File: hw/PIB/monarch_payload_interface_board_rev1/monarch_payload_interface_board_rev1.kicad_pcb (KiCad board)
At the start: 4 copper layers, 96 x 89.9 mm, 187 parts, among them J1 5037630291, J10 5037630491, J11 5037630691, J12 5037630691, J13 5037630491, J14 5037630491, J15 5037630691, J16 20021121-00008C4LF, J2 5037630291, J3 5037630691, J4 5037630691, J5 5037630691, J6 5037630691, J7 5037630691, J8 5037630691, J9 5037630491, Q1 FZT600TA, Q10 FZT600TA, Q11 FZT600TA, Q12 FZT600TA, Q13 FZT600TA, Q14 FZT600TA, Q15 FZT600TA, Q16 FZT600TA, Q17 FZT600TA, Q18 FZT600TA, Q19 FZT600TA, Q2 FZT600TA, Q3 FZT600TA, Q4 FZT600TA, Q5 FZT600TA, Q6 FZT600TA, Q7 FZT600TA, Q8 FZT600TA, Q9 FZT600TA, U1 Payload, U10 AD7124-8BCPZ-RL, U11 WSK06121L000FEA, U12 WSK06121L000FEA, U13 WSK06121L000FEA, U14 WSK06121L000FEA, U2 STM32L4A6VGTx, U3 MAX31856MUD_T, U4 TPS61088QRHLRQ1, U5 MAX31856MUD_T, U6 MAX31856MUD_T, U7 MAX31856MUD_T, U8 MAX31856MUD_T, U9 AD7124-8BCPZ-RL

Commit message: more minor tweaks
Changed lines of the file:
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@@
 		(polygon
 			(pts
-				(xy 51.29 70.12) (xy 51.29 83.17) (xy 51.04 83.42) (xy 51.04 101.62) (xy 51.06 101.64) (xy 121.15 101.64)
+				(xy 51.29 70.12) (xy 50.95 82.55) (xy 50.59 83.87) (xy 50.59 101.17) (xy 51.06 101.64) (xy 121.15 101.64)
 				(xy 121.51 101.28) (xy 121.51 70.69) (xy 64.88 70.69) (xy 62.9 72.67) (xy 55.73 72.67) (xy 53.57 70.51)
 				(xy 53.57 70.12)
@@
 			(pts
 				(xy 62.9832 46.3172) (xy 67.6314 46.3172) (xy 67.6568 46.2918) (xy 67.6568 42.8882) (xy 67.6314 42.8628)
-				(xy 65.7518 42.8628) (xy 64.2532 41.3642) (xy 64.05 41.3642) (xy 64.05 42.1516) (xy 63.923 42.2786)
+				(xy 65.7518 42.8628) (xy 64.2532 41.3642) (xy 64.05 41.3642) (xy 64.05 41.9516) (xy 63.723 42.2786)
 				(xy 62.9832 42.2786)
 			)

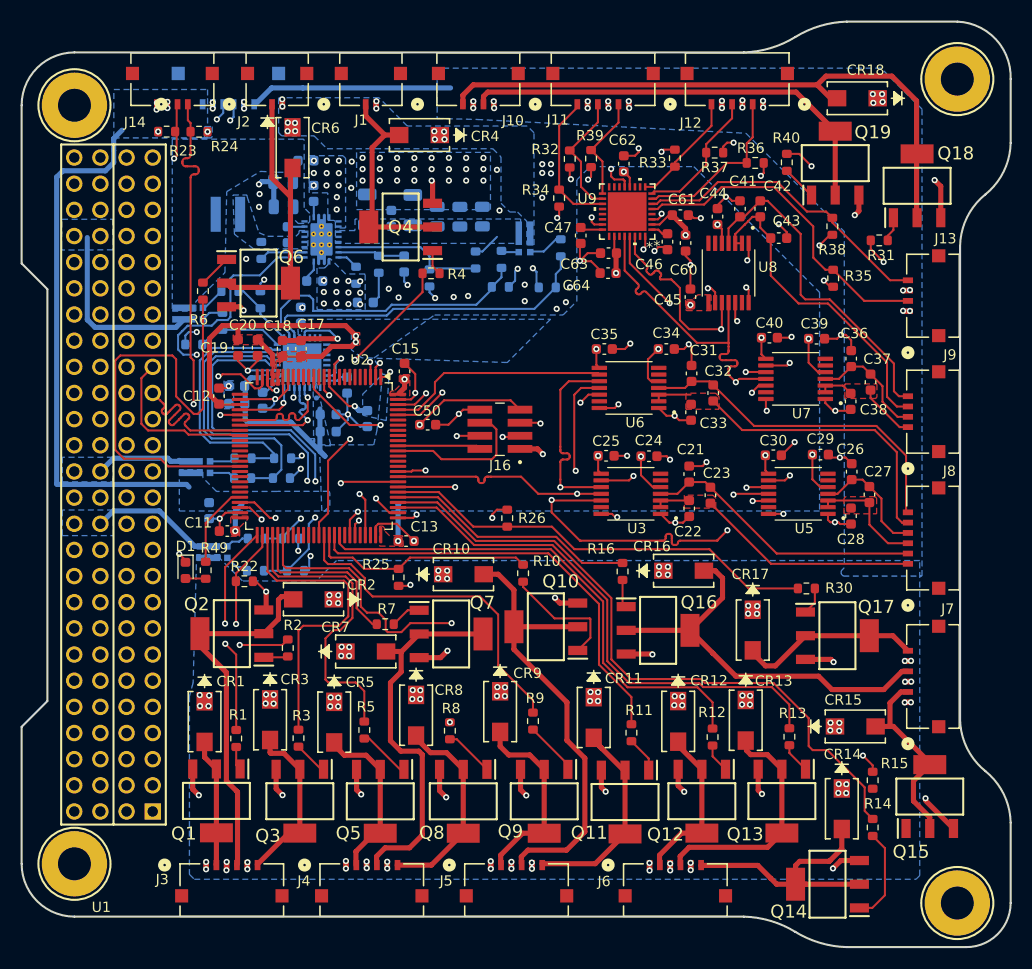
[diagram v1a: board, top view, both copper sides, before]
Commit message: fixed vias
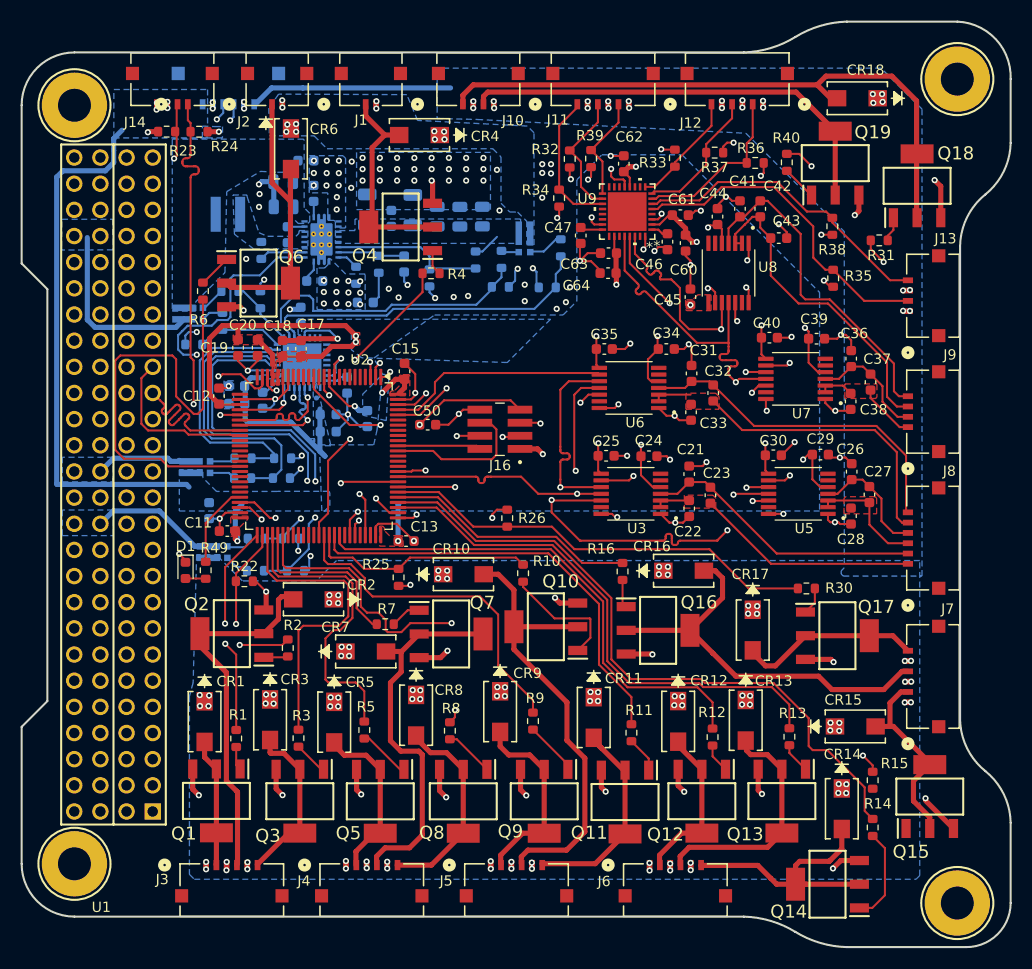
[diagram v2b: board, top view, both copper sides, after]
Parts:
- R49: value 1k -> 125
- moved CR6 0.19 mm to (60.5, 30.7)
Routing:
- net +3V3: track 164.7 -> 187.2 mm

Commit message: PIB Signature
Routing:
- net GND: vias 154 -> 156
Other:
- board text added: "MonARCH Payload Interface Board Rev. 1 SIROTA 3/12/2026"
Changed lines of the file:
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@@
 		(tags "capacitor")
 		(property "Reference" "C15"
-			(at 2.185 0.08 0)
+			(at -0.235 2.52 0)
 			(layer "F.SilkS")
 			(effects
@@
 		)
 	)
+	(gr_rect
+		(start 68.25 47)
+		(end 87.75 50.4)
+		(stroke
+			(width 0.1)
+			(type default)
+		)
+		(fill no)
+		(layer "F.SilkS")
+	)
+	(gr_text "MonARCH Payload Interface Board Rev. 1\nSIROTA 3/12/2026"
+		(at 78 49.95 0)
+		(layer "F.SilkS")
+		(effects
+			(font
+				(size 0.9 0.6)
+				(thickness 0.15)
+			)
+			(justify bottom)
+		)
+	)
 	(segment
 		(start 61.74712 38.2778)
@@
 	)
 	(via
+		(at 80.4 34.5)
+		(size 0.6)
+		(drill 0.3)
+		(layers "F.Cu" "B.Cu")
+		(free yes)
+		(net 3)
+	)
+	(via
 		(at 83.9402 42.306)
 		(size 0.6)
@@
 		(net 3)
 	)
+	(via
+		(at 85.15 30.9)
+		(size 0.6)
+		(drill 0.3)
+		(layers "F.Cu" "B.Cu")
+		(free yes)
+		(net 3)
+	)

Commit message: Pinouts Sheet
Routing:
- net Net-(Q15-B): track 0.00 -> 5.20 mm
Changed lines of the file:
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@@
 		(tenting front back)
 		(pcbplotparams
-			(layerselection 0x00000000_00000000_55555555_5755f5ff)
+			(layerselection 0x00000000_00000000_55555555_5555f500)
 			(plot_on_all_layers_selection 0x00000000_00000000_00000000_00000000)
 			(disableapertmacros no)
@@
 			(psa4output no)
 			(plot_black_and_white yes)
-			(sketchpadsonfab no)
+			(sketchpadsonfab yes)
 			(plotpadnumbers no)
 			(hidednponfab no)
@@
 			(outputformat 1)
 			(mirror no)
-			(drillshape 1)
+			(drillshape 0)
 			(scaleselection 1)
 			(outputdirectory "")
@@
 	)
 	(segment
+		(start 116.94 92.85)
+		(end 116.94 93.47)
+		(width 0.2)
+		(layer "F.Cu")
+		(net 66)
+	)
+	(segment
+		(start 116.94 93.47)
+		(end 120.18 96.71)
+		(width 0.2)
+		(layer "F.Cu")
+		(net 66)
+	)
+	(segment
